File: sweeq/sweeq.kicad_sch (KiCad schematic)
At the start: 74 parts, among them J1 MJ-4PP-9, J2 MJ-4PP-9, SW1 SW_PUSH, SW10 SW_PUSH, SW11 SW_PUSH, SW12 SW_PUSH, SW13 SW_PUSH, SW14 SW_PUSH, SW15 SW_PUSH, SW16 SW_PUSH, SW17 SW_PUSH, SW18 SW_PUSH, SW19 SW_PUSH, SW2 SW_PUSH, SW20 SW_PUSH, SW21 SW_PUSH, SW22 SW_PUSH, SW23 SW_PUSH, SW24 SW_PUSH, SW25 SW_PUSH, SW26 SW_PUSH, SW27 SW_PUSH, SW28 SW_PUSH, SW29 SW_PUSH, SW3 SW_PUSH, SW30 SW_PUSH, SW31 SW_PUSH, SW32 SW_PUSH, SW33 SW_PUSH, SW34 SW_PUSH, SW4 SW_PUSH, SW5 SW_PUSH, SW6 SW_PUSH, SW7 SW_PUSH, SW8 SW_PUSH, SW9 SW_PUSH, U1 ProMicro, U2 ProMicro

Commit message: rename sweep to sweeq
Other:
- company: foostan -> idank
- title: Corne Light -> sweeq

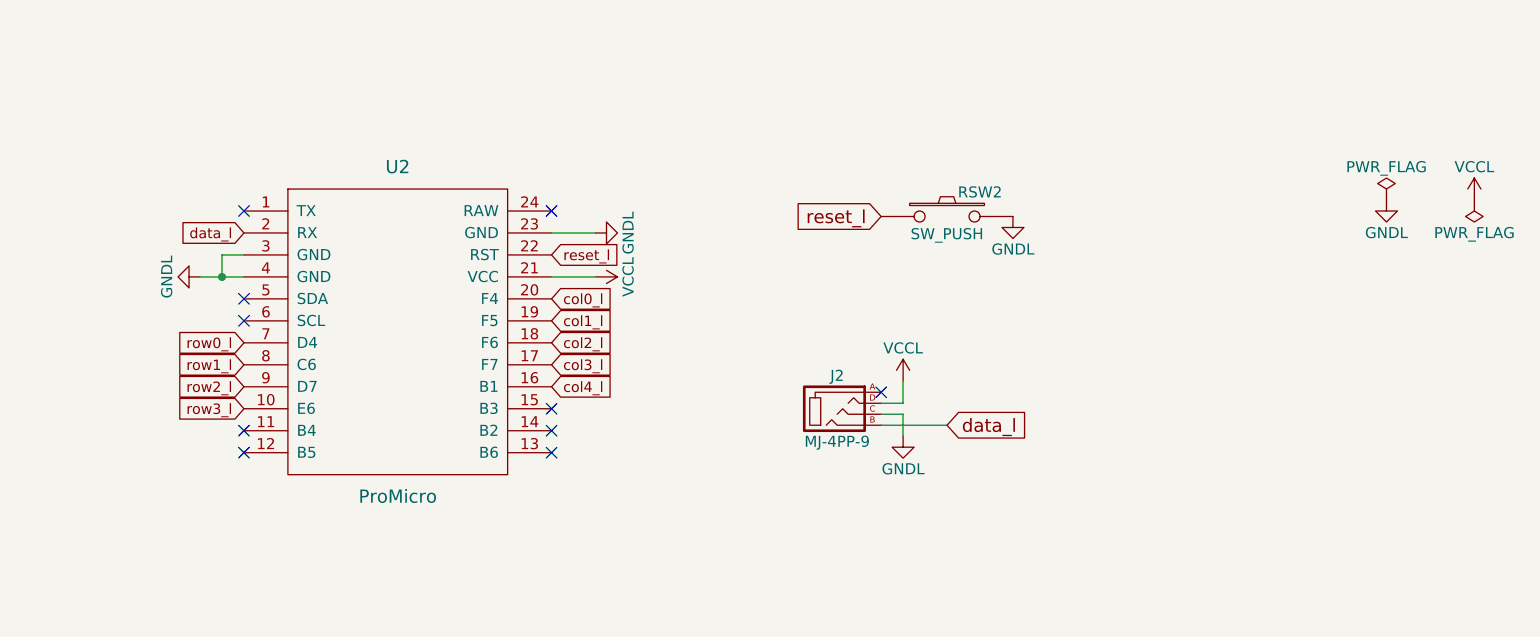
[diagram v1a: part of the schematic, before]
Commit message: sweeq: fix left side tenting holes being 1mm off
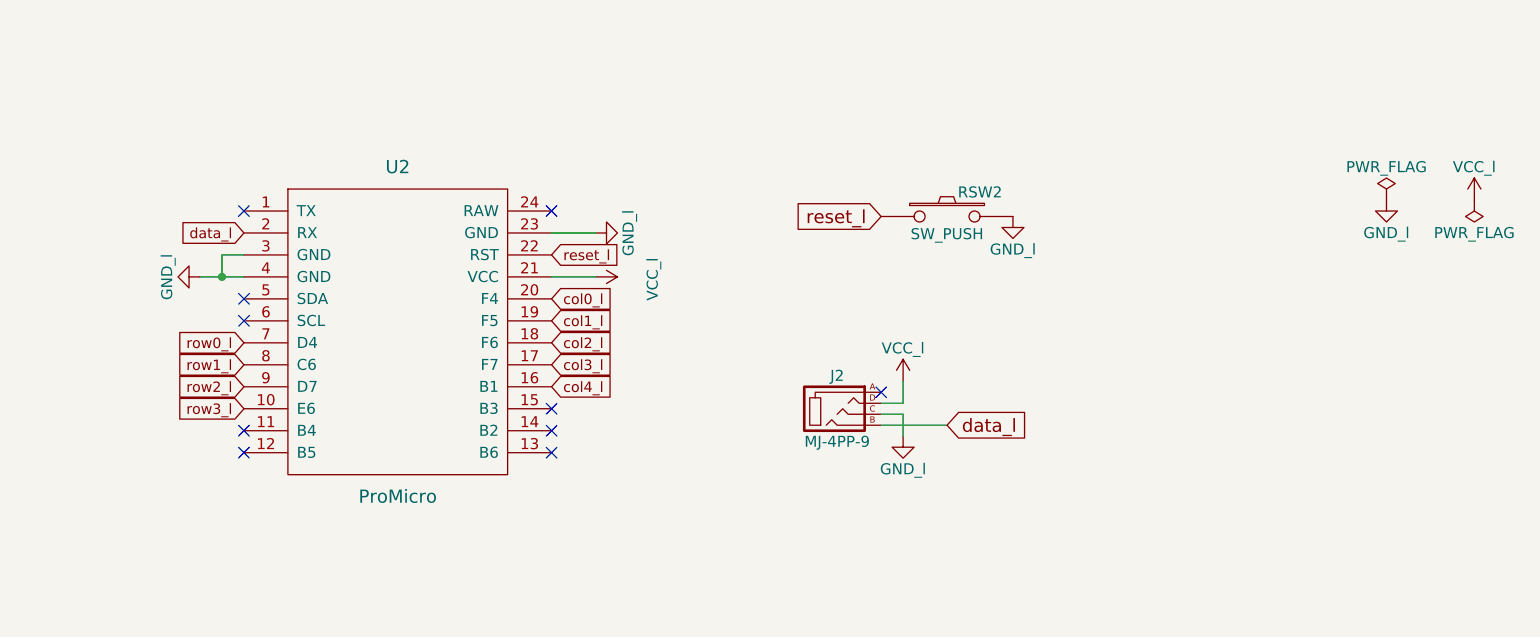
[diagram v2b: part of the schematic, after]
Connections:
- net GND: no longer J2.C, RSW2.2, U2.23 (GND), U2.3 (GND), U2.4 (GND)
- net VCC: no longer J2.D, U2.21 (VCC)
- new net GND_l: J2.C, RSW2.2, U2.23 (GND), U2.3 (GND), U2.4 (GND)
- new net VCC_l: J2.D, U2.21 (VCC)
